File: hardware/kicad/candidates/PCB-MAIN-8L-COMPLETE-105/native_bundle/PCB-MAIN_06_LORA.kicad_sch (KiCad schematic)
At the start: 19 parts, among them J10 U.FL-R-SMT-1(60), U10 E22-900M22S

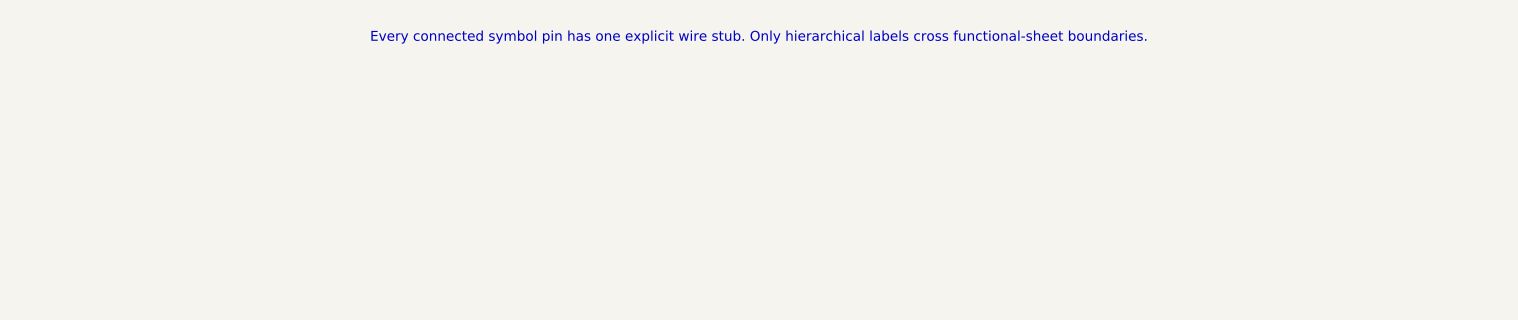
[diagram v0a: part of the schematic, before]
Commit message: PCB-MAIN Rev B: bilingual schematic notes and PDF
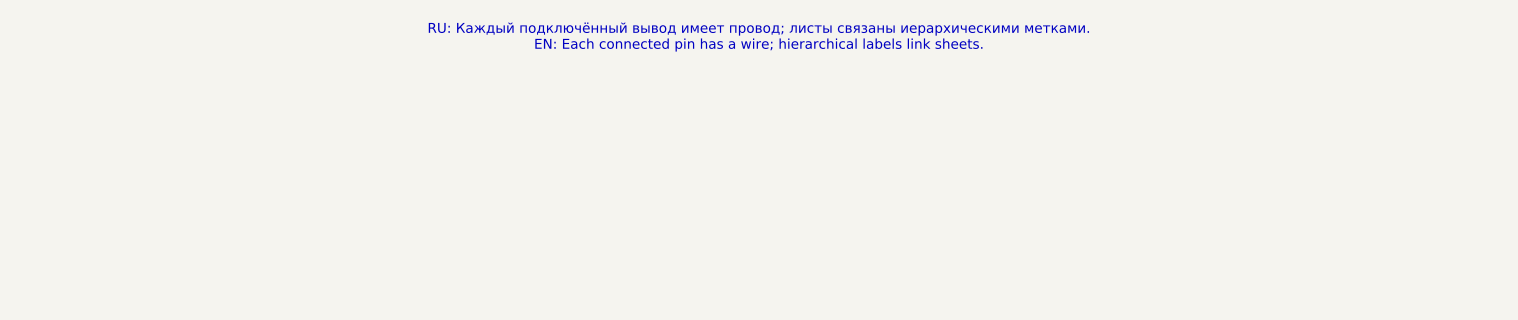
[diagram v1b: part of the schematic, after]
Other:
- note added: "RU: Каждый подключённый вывод имеет провод; листы связаны иерархическими метками. EN: Each connected pin has a wire; hierarchical labels link sheets."
- note removed: "Every connected symbol pin has one explicit wire stub. Only hierarchical labels cross functional-sheet boundaries."
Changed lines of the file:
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@@
     (stroke (width 0.0))
   )
-  (text "Every connected symbol pin has one explicit wire stub. Only hierarchical labels cross functional-sheet boundaries."
+  (text "RU: Каждый подключённый вывод имеет провод; листы связаны иерархическими метками.\nEN: Each connected pin has a wire; hierarchical labels link sheets."
     (at 297.0 12.7 0)
     (effects (font (size 1.1 1.1)))
